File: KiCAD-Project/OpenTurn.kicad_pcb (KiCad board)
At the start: 4 copper layers, 66 x 84.5 mm, 152 parts, among them J201 XT30, J202 Conn_02x04_Odd_Even, J203 Conn_01x03_Shielded, J204 Conn_01x03_Shielded, J301 GPIOs, J302 JTAG/SWD, J303 Conn_01x03_Shielded, Q501 IAUC120N06S5N017ATMA1, Q502 IAUC120N06S5N017ATMA1, Q601 IAUC120N06S5N017ATMA1, Q602 IAUC120N06S5N017ATMA1, Q701 IAUC120N06S5N017ATMA1, Q702 IAUC120N06S5N017ATMA1, U201 TI_TCAN337G, U202 TLE5012B_E1000, U203 MAX15062A, U301 CY8C6244AZI-S4D92, U302 MCP9700AT-HTT, U401 DRV8323SRTAR-DRV8323SRTAR, Y301 32MHz

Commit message: fixing DRC
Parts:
- added NT101: Net-Tie_2, NetTie:NetTie-2_SMD_Pad0.5mm, F.Cu at (176.7, 101.0)
- added NT102: Net-Tie_2, NetTie:NetTie-2_SMD_Pad0.5mm, F.Cu at (173.6, 101.0)
- TP401: renamed from TP404; value DRV_CS -> MOSI
- TP402: renamed from TP403; value SPI_SCK -> MISO
- TP403: renamed from TP401; value MOSI -> SPI_SCK
- TP404: renamed from TP402; value MISO -> DRV_CS
- moved R303 12.5 mm to (141.3, 101.8), turned to 180 degrees
- moved R302 10.9 mm to (141.3, 100.3), turned to 180 degrees
- moved TP205 7.65 mm to (152.3, 128.7), turned to -90 degrees
- moved TP206 7.64 mm to (152.3, 131.2)
- moved R206 4.67 mm to (148.3, 97.0), turned to -90 degrees
- moved TP201 2.15 mm to (152.3, 126.2), turned to -90 degrees
- moved TP204 2.14 mm to (152.3, 123.7)
- moved C409 1.46 mm to (117.4, 119.0), turned to 90 degrees
- moved L302 1.15 mm to (126.8, 103.2)
- moved TP202 0.88 mm to (130.4, 95.3)
- moved R203 0.70 mm to (136.1, 95.5)
- moved C401 0.48 mm to (134.6, 122.6)
- moved C404 0.48 mm to (131.7, 122.6)
- moved C402 0.48 mm to (133.2, 122.6)
- moved C406 0.47 mm to (130.2, 122.6)
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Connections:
- net /MCU/RESET renamed /Interfaces/RESET
- H103 pad 1: unconnected-(H103-Pad1) -> (no net)
- J202 pad 1: +3V3 -> /Interfaces/ENCODER_QOAD_I2
- J202 pad 2: GNDS -> /Interfaces/ENCODER_CS1
- J202 pad 3: /Interfaces/ENCODER_DATA -> /Interfaces/ENCODER_QOAD_B2
- J202 pad 4: /Interfaces/ENCODER_QOAD_A2 -> /Interfaces/ENCODER_SCK
- J202 pad 5: /Interfaces/ENCODER_SCK -> /Interfaces/ENCODER_QOAD_A2
- J202 pad 6: /Interfaces/ENCODER_QOAD_B2 -> /Interfaces/ENCODER_DATA
- J202 pad 7: /Interfaces/ENCODER_CS1 -> GNDS
- J202 pad 8: /Interfaces/ENCODER_QOAD_I2 -> +3V3
- J302 pad 8: unconnected-(J302-Pad8) -> (no net)
- TP401 pad 1: /MCU/DRV_CS -> /MCU/DRV_MOSI
- TP402 pad 1: /MCU/DRV_SCK -> /MCU/DRV_MISO
- TP403 pad 1: /MCU/DRV_MOSI -> /MCU/DRV_SCK
- TP404 pad 1: /MCU/DRV_MISO -> /MCU/DRV_CS
- U201 pad 8: unconnected-(U201-Pad8) -> (no net)
- U301 pad 16: unconnected-(U301-Pad16) -> (no net)
- U301 pad 26: unconnected-(U301-Pad26) -> (no net)
- U301 pad 27: unconnected-(U301-Pad27) -> (no net)
- U301 pad 29: unconnected-(U301-Pad29) -> (no net)
- U301 pad 33: unconnected-(U301-Pad33) -> /MCU/DRV_PWM_AL
- U301 pad 34: unconnected-(U301-Pad34) -> /MCU/DRV_PWM_AH
- U301 pad 35: /MCU/DRV_SCK -> /MCU/DRV_PWM_BL
- U301 pad 36: /MCU/DRV_CS -> /MCU/DRV_PWM_BH
- U301 pad 37: /MCU/DRV_MOSI -> /MCU/DRV_PWM_CL
- U301 pad 38: /MCU/DRV_MISO -> /MCU/DRV_PWM_CH
- U301 pad 39: /MCU/DRV_PWM_AL -> /MCU/DRV_MOSI
- U301 pad 40: /MCU/DRV_PWM_AH -> /MCU/DRV_MISO
- U301 pad 41: /MCU/DRV_PWM_BL -> /MCU/DRV_SCK
- U301 pad 42: /MCU/DRV_PWM_BH -> /MCU/DRV_CS
- U301 pad 43: /MCU/DRV_PWM_CL -> /MCU/DRV_CAL
- U301 pad 44: /MCU/DRV_PWM_CH -> (no net)
- U301 pad 48: /MCU/DRV_CAL -> (no net)
- U301 pad 55: unconnected-(U301-Pad55) -> (no net)
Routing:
- net Net-(D302-Pad2): track 1.39 -> 17.1 mm
- net /MCU/STATUS_LED0: track 18.7 -> 3.02 mm
- net Net-(D301-Pad2): track 1.39 -> 16.1 mm
- net /MCU/STATUS_LED1: track 18.3 -> 4.77 mm
- net /MCU/DRV_SCK: track 37.8 -> 28.8 mm, vias 2 -> 3
- net /Interfaces/ENCODER_QOAD_B1: track 46.7 -> 55.0 mm
- net /Interfaces/ENCODER_QOAD_I1: track 40.1 -> 47.7 mm
- net /MCU/DRV_PWM_CH: track 10.7 -> 17.8 mm
- net /MCU/DRV_PWM_BL: track 14.6 -> 21.5 mm
- net /MCU/DRV_PWM_CL: track 11.5 -> 18.4 mm
- net VDD: track 45.8 -> 51.6 mm, vias 9 -> 11
- net /MCU/DRV_PWM_BH: track 13.8 -> 19.0 mm
- net Net-(D201-Pad2): track 1.39 -> 5.97 mm
- net /MCU/DRV_CS: track 33.5 -> 29.2 mm, vias 2 -> 3
- net /MCU/DRV_PWM_AH: track 16.3 -> 20.3 mm
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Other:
- board text added: "3V3"

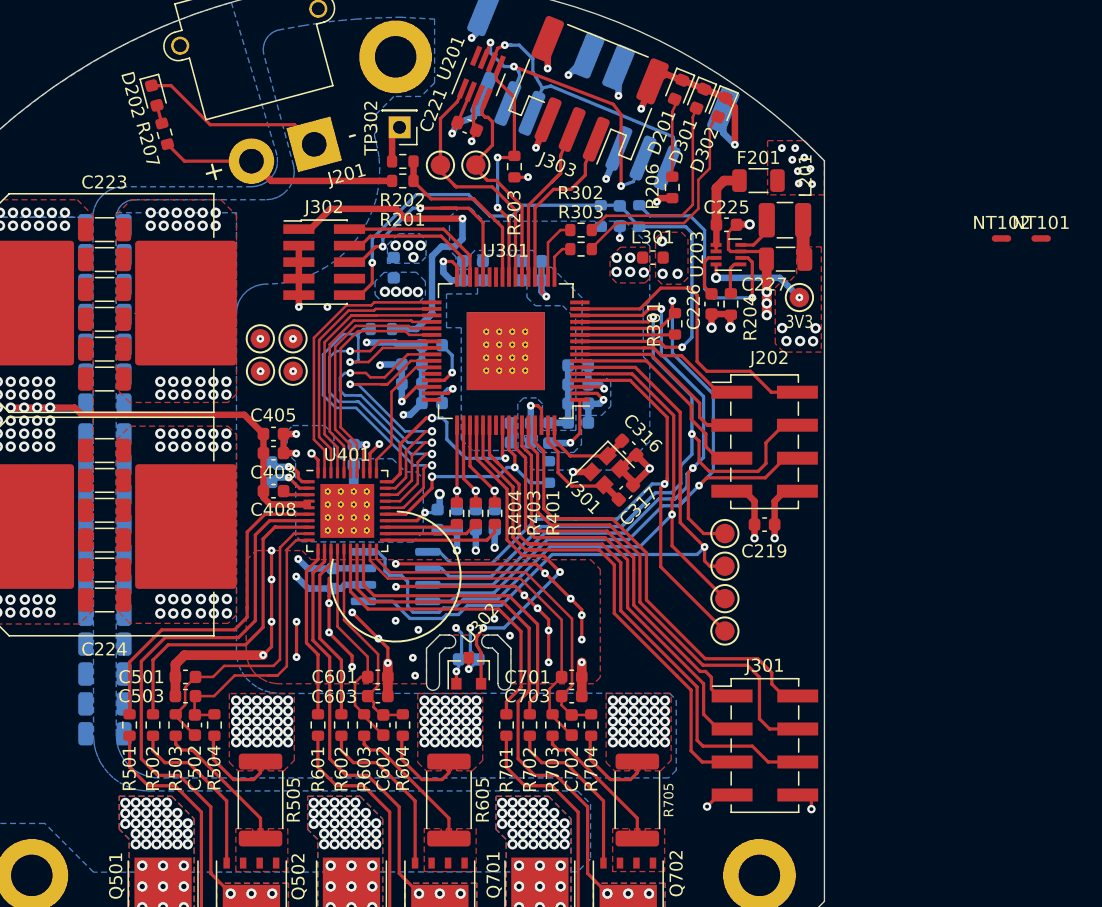
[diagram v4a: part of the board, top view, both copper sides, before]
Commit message: DRC resolved
removed GNDA, GNDS from schematic due to no solution was found to get a net-tie in inner layers
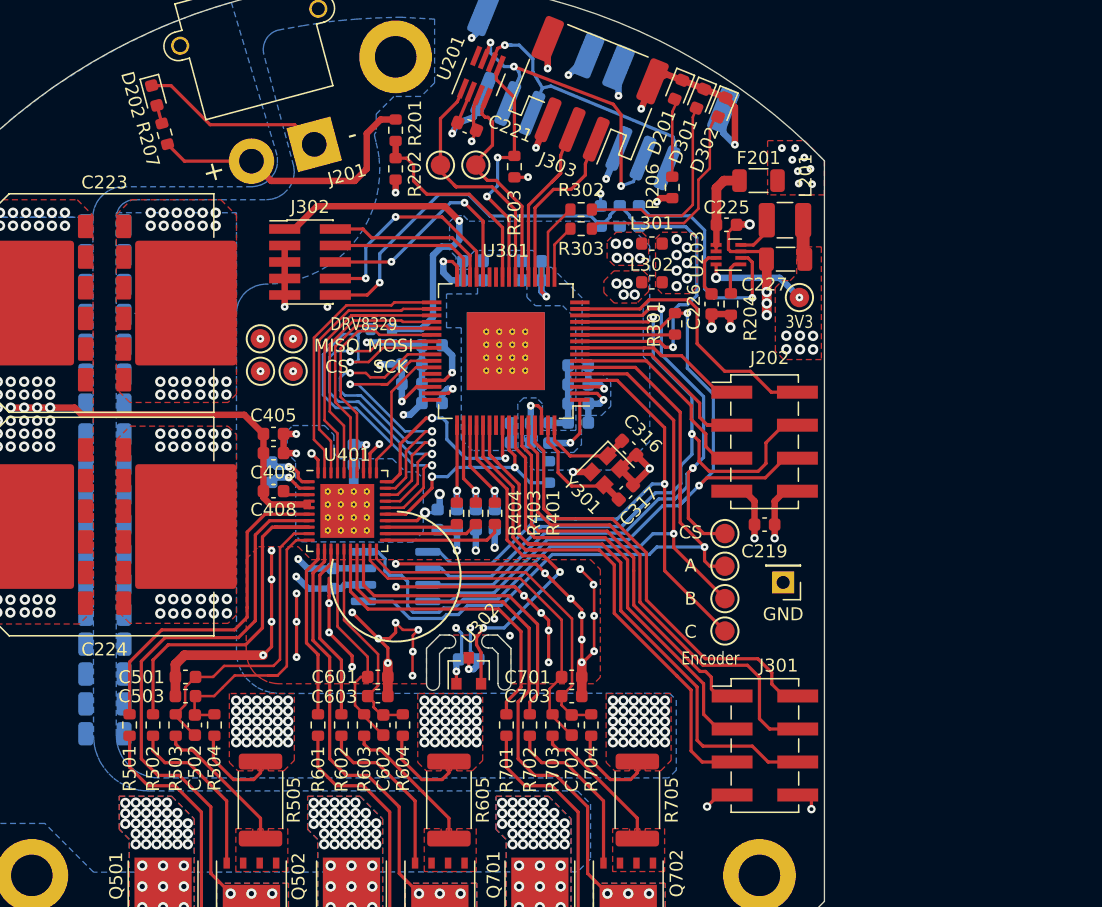
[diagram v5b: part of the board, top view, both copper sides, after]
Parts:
- removed C220, C228, C229, C230, C231, C232, C233, C234, C235, C236, C237, C238: 10u, Capacitor_SMD:C_1206_3216Metric
- removed NT101, NT102: Net-Tie_2, NetTie:NetTie-2_SMD_Pad0.5mm
- L302: moved to F.Cu
- moved TP302 45.8 mm to (156.8, 127.4)
- moved L302 19.9 mm to (146.7, 104.3), turned to 180 degrees
- moved R201 3.94 mm to (127.0, 92.7), turned to 90 degrees
- moved R302 1.58 mm to (141.3, 98.8)
- moved R303 1.58 mm to (141.3, 100.2)
- moved C318 1.46 mm to (142.8, 99.2), turned to 90 degrees
- moved R305 1.46 mm to (144.2, 99.2)
- moved J302 1.09 mm to (120.4, 102.8)
- moved L301 1.08 mm to (146.7, 101.4)
- moved R202 0.80 mm to (127.0, 95.6), turned to -90 degrees
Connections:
- C219 pad 2: GNDS -> GND
- C221 pad 2: GNDS -> GND
- C222 pad 2: GNDS -> GND
- C225 pad 2: GNDS -> GND
- C226 pad 2: GNDS -> GND
- C227 pad 2: GNDS -> GND
- C301 pad 2: GNDS -> GND
- C302 pad 2: GNDA -> GND
- C303 pad 2: GNDS -> GND
- C304 pad 2: GNDA -> GND
- C305 pad 2: GNDS -> GND
- C306 pad 2: GNDS -> GND
- C307 pad 2: GNDS -> GND
- C308 pad 2: GNDS -> GND
- C309 pad 2: GNDS -> GND
- C310 pad 2: GNDS -> GND
- C311 pad 2: GNDA -> GND
- C312 pad 2: GNDA -> GND
- C313 pad 2: GNDS -> GND
- C314 pad 2: GNDS -> GND
- C315 pad 2: GNDS -> GND
- C316 pad 2: GNDS -> GND
- C317 pad 2: GNDS -> GND
- C318 pad 2: GNDS -> GND
- C322 pad 2: GNDA -> GND
- C401 pad 2: GNDA -> GND
- C402 pad 2: GNDA -> GND
- C404 pad 2: GNDA -> GND
- C406 pad 2: GNDA -> GND
- C501 pad 2: GNDA -> GND
- C503 pad 2: GNDA -> GND
- C601 pad 2: GNDA -> GND
- C603 pad 2: GNDA -> GND
- C701 pad 2: GNDA -> GND
- C703 pad 2: GNDA -> GND
- D201 pad 1: GNDS -> GND
- D301 pad 1: GNDS -> GND
- D302 pad 1: GNDS -> GND
- H101 pad 1: GNDS -> GND
- H103 pad 1: (no net) -> unconnected-(H103-Pad1)
- J202 pad 7: GNDS -> GND
- J203 pad 1: GNDS -> GND
- J203 pad SH: GNDS -> GND
- J204 pad 1: GNDS -> GND
- J204 pad SH: GNDS -> GND
- J301 pad 8: GNDS -> GND
- J302 pad 3: GNDS -> GND
- J302 pad 5: GNDS -> GND
- J302 pad 7: GNDS -> GND
- J302 pad 8: (no net) -> /MCU/TDI
- J302 pad 9: GNDS -> GND
- J303 pad 3: GNDS -> GND
- J303 pad SH: GNDS -> GND
- R202 pad 2: GNDS -> GND
- R204 pad 2: GNDS -> GND
- TP302 pad 1: GNDS -> GND
- U201 pad 2: GNDS -> GND
- U201 pad 8: (no net) -> unconnected-(U201-Pad8)
- U202 pad 7: GNDS -> GND
- U203 pad 7: GNDS -> GND
- U301 pad 16: (no net) -> unconnected-(U301-Pad16)
- U301 pad 26: (no net) -> unconnected-(U301-Pad26)
- U301 pad 27: (no net) -> unconnected-(U301-Pad27)
- U301 pad 29: (no net) -> /MCU/TDI
- U301 pad 44: (no net) -> unconnected-(U301-Pad44)
- U301 pad 48: (no net) -> unconnected-(U301-Pad48)
- U301 pad 55: (no net) -> unconnected-(U301-Pad55)
- U301 pad 65: GNDS -> GND
- U302 pad 3: GNDA -> GND
- U401 pad 32: GNDA -> GND
- Y301 pad 2: GNDS -> GND
- Y301 pad 4: GNDS -> GND
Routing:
- net GND: track 46.3 -> 270.6 mm, vias 141 -> 207
- net GNDS: track 109.7 -> 0.00 mm, vias 23 -> 0
- net GNDA: track 96.3 -> 0.00 mm, vias 37 -> 0
- net /MCU/TDI: track 0.00 -> 17.3 mm, vias 0 -> 2
- net VBUS: track 47.8 -> 51.6 mm
- net /Power/Sheet61668C54/FET_GL: track 24.6 -> 27.3 mm
- net /Interfaces/V_BUS_SENSE: track 13.7 -> 16.3 mm
- net /Interfaces/ENCODER_CS1: track 23.7 -> 21.6 mm
- net /Interfaces/RESET: track 50.8 -> 52.2 mm
- net +3V3: track 61.8 -> 63.2 mm, vias 20 -> 21
- net /Interfaces/ENCODER_DATA: track 58.8 -> 57.5 mm
- net /MCU/STATUS_LED0: track 3.02 -> 4.23 mm
- net /MCU/STATUS_LED1: track 4.77 -> 5.91 mm
- net /MCU/SWDIO: track 11.8 -> 12.9 mm
- net /Interfaces/ENCODER_QOAD_I1: track 47.7 -> 46.7 mm
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- added copper zone on F.Cu, net VDDA
- removed copper zone on B.Cu, net +3V3
- removed copper zone on F.Cu, net GNDA
- removed copper zone on In1.Cu, net GNDA
- removed copper zone on B.Cu, net GNDS
- removed copper zone on In1.Cu, net GNDS
- removed copper zone on B.Cu, net VDDA
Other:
- board text added: "A"
- board text added: "B"
- board text added: "C"
- board text added: "CS"
- board text added: "DRV8329"
- board text added: "Encoder"
- board text added: "GND"
- board text added: "MISO"
- board text added: "MOSI"
- board text added: "SCK"

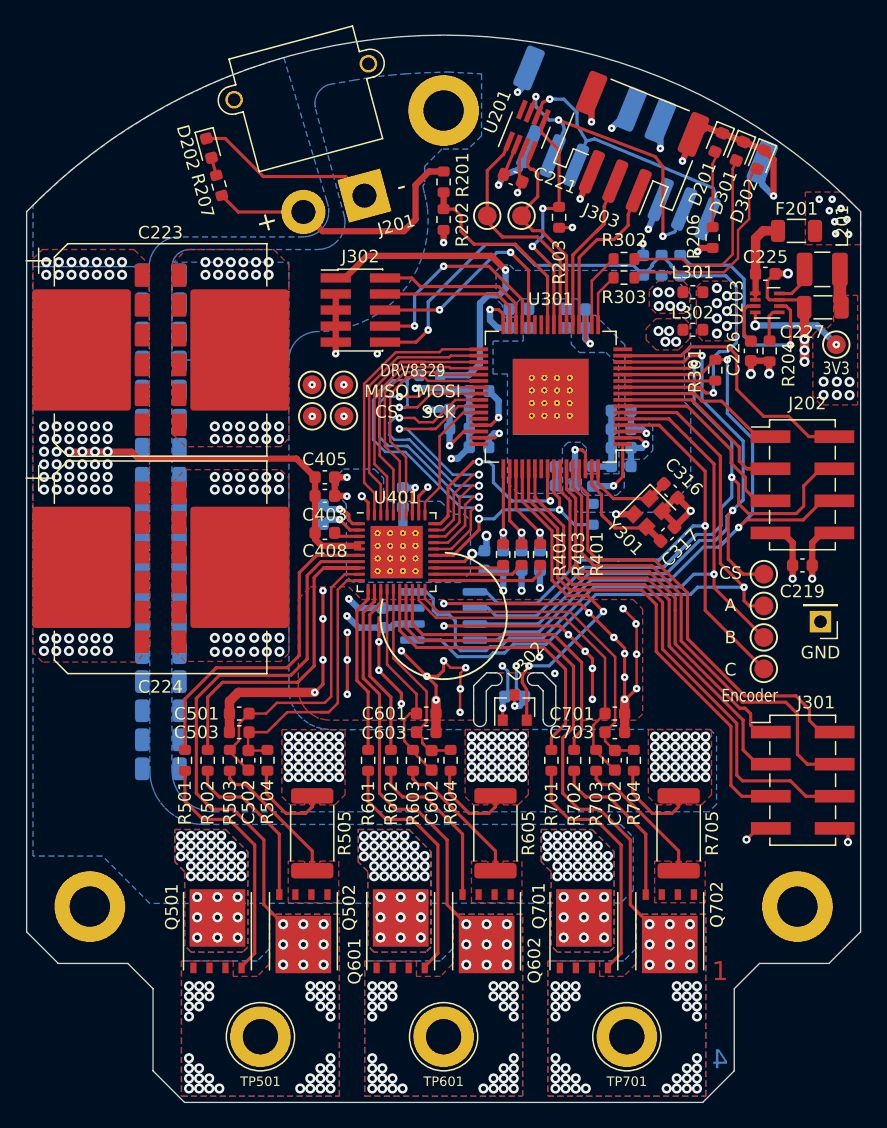
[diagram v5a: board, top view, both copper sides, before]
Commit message: DRC passed
1 error still reported due to placeholder in silkscreen
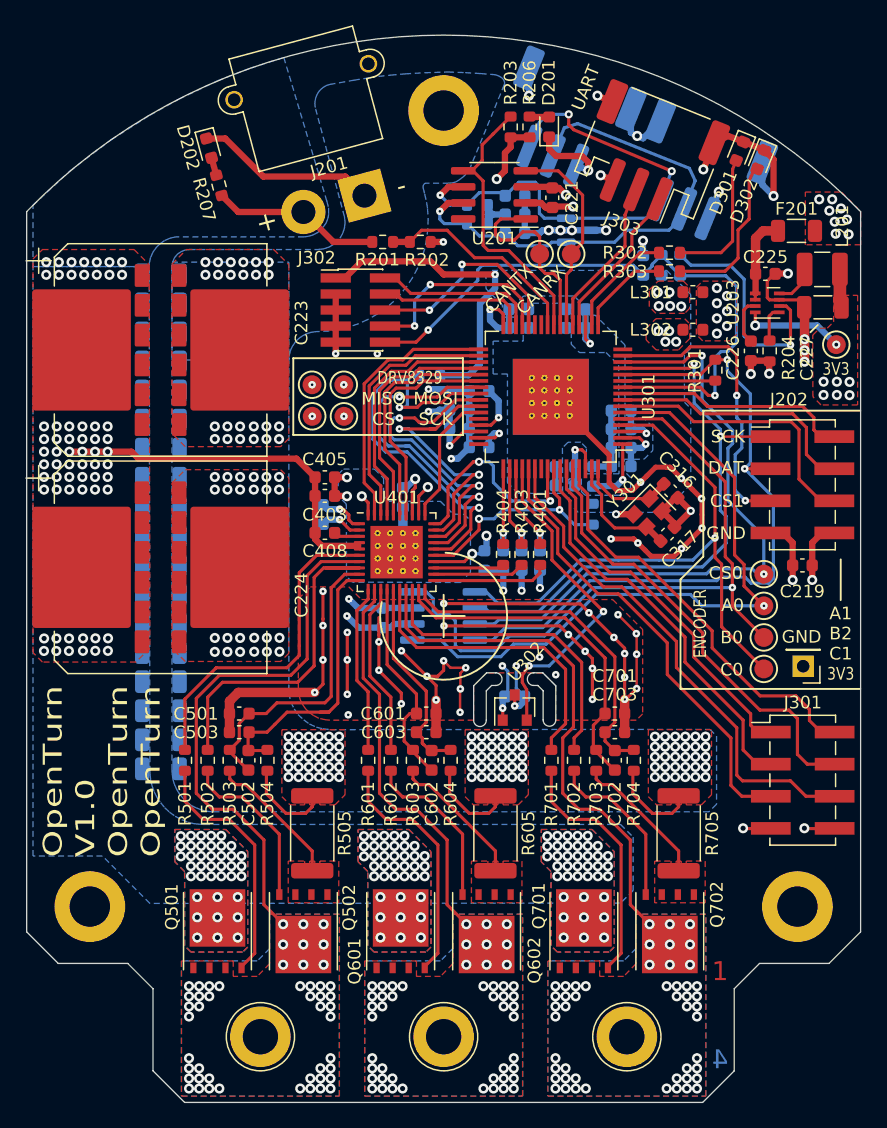
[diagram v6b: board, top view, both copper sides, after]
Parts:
- added C1: 100n, Capacitor_SMD:C_0603_1608Metric, B.Cu at (132.6, 95.2)
- added C2: 100n, Capacitor_SMD:C_0603_1608Metric, B.Cu at (132.7, 96.7)
- added C3: 100n, Capacitor_SMD:C_0603_1608Metric, B.Cu at (132.7, 93.8)
- added D1: NUP2105L, Package_TO_SOT_SMD:SOT-23, B.Cu at (137.6, 96.5)
- added R1: 60R, Resistor_SMD:R_0603_1608Metric, B.Cu at (129.7, 96.0)
- added R2: 60R, Resistor_SMD:R_0603_1608Metric, B.Cu at (129.7, 94.5)
- U201: footprint Package_TO_SOT_SMD:SOT-23-8_Handsoldering -> Package_SO:SOIC-8_3.9x4.9mm_P1.27mm
- moved R206 16.9 mm to (133.8, 88.3)
- moved D201 13.5 mm to (135.3, 88.3), turned to 90 degrees
- moved R203 8.12 mm to (132.3, 88.3)
- moved R201 6.77 mm to (122.2, 97.4), turned to 180 degrees
- moved U201 5.74 mm to (131.0, 93.7), turned to 180 degrees
- moved TP202 5.14 mm to (134.6, 98.4)
- moved TP203 4.96 mm to (137.1, 98.3)
- moved TP302 3.78 mm to (155.4, 131.0)
- moved R302 3.64 mm to (144.9, 98.2)
- moved R303 3.64 mm to (144.9, 99.7)
- moved C221 3.47 mm to (135.6, 93.9), turned to -90 degrees
- moved R202 2.56 mm to (125.2, 97.4), turned to 0 degrees
- moved J303 1.78 mm to (143.3, 90.6)
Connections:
- J202 pad 1: /Interfaces/ENCODER_QOAD_I2 -> /Interfaces/ENCODER_SCK
- J202 pad 2: /Interfaces/ENCODER_CS1 -> /Interfaces/ENCODER_QOAD_I2
- J202 pad 3: /Interfaces/ENCODER_QOAD_B2 -> /Interfaces/ENCODER_DATA
- J202 pad 4: /Interfaces/ENCODER_SCK -> /Interfaces/ENCODER_QOAD_B2
- J202 pad 5: /Interfaces/ENCODER_QOAD_A2 -> /Interfaces/ENCODER_CS1
- J202 pad 6: /Interfaces/ENCODER_DATA -> /Interfaces/ENCODER_QOAD_A2
- J203 pad 1: GND -> Net-(C3-Pad1)
- J203 pad 3: Net-(J203-Pad3) -> GND
- J204 pad 1: GND -> Net-(C3-Pad1)
- J204 pad 3: Net-(J203-Pad3) -> GND
- U201 pad 6: Net-(J203-Pad3) -> Net-(C3-Pad1)
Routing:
- net Net-(C3-Pad1): track 0.00 -> 40.9 mm, vias 0 -> 3
- net GND: track 270.6 -> 306.0 mm, vias 207 -> 219
- net Net-(J203-Pad3): track 22.8 -> 0.00 mm, vias 1 -> 0
- net Net-(C2-Pad1): track 25.2 -> 41.1 mm, vias 3 -> 1
- net /Interfaces/ENCODER_SCK: track 57.9 -> 47.3 mm
- net VBUS: track 51.6 -> 42.7 mm
- net /Interfaces/ENCODER_QOAD_A2: track 16.0 -> 22.1 mm
- net /Interfaces/ENCODER_QOAD_I2: track 13.1 -> 18.7 mm
- net /Interfaces/ENCODER_QOAD_B2: track 15.3 -> 20.2 mm
- net Net-(D301-Pad2): track 15.8 -> 11.0 mm
- net Net-(C1-Pad1): track 0.00 -> 4.64 mm
- net Net-(D201-Pad2): track 5.97 -> 1.52 mm
- net /Interfaces/CANFD_Fault: track 19.2 -> 23.5 mm, vias 2 -> 0
- net /Interfaces/CANFD_TX: track 19.4 -> 15.5 mm
- net Net-(D302-Pad2): track 16.4 -> 12.6 mm
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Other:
- board text added: "48V 20A"
- board text added: "A0"
- board text added: "A1"
- board text added: "B0"
- board text added: "B2"
- board text added: "C0"
- board text added: "C1"
- board text added: "C201"
- board text added: "C218"
- board text added: "CAN"
- board text added: "CANRX"
- board text added: "CANTX"
- board text added: "CS0"
- board text added: "CS1"
- board text added: "DAT"
- board text added: "ENCODER"
- board text added: "OpenTurn"
- board text added: "UART"
- board text added: "V1.0"
- board text removed: "A"
- board text removed: "B"
- board text removed: "C"
- board text removed: "Encoder"

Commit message: added brd pdf
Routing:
- net GND: vias 219 -> 242
